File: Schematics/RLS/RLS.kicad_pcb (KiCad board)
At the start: 4 copper layers, 228.6 x 228.6 mm, 121 parts, among them J1 Velleman_Probe1, J2 Velleman_Probe2, J3 Velleman_FuncGen, J4 Logic_Analyzer1, J5 Logic_Analyzer2, J6 ADS1115, J7 DC_Fan, Q1 BS170, U1 ARDUINO_MEGA_SHIELD, U10 LT1963, U11 LT1963, U12 ULN2803A, U13 RA30421051, U14 RA30421051, U15 RB496EATR, U16 RB496EATR, U17 NE5532, U18 NE5532, U19 RB496EATR, U2 LM317T, U20 RB496EATR, U21 NE5532, U3 LM337T, U4 AD5293, U5 AD5293, U6 LT3015, U7 LT3015, U8 AD5293, U9 AD5293

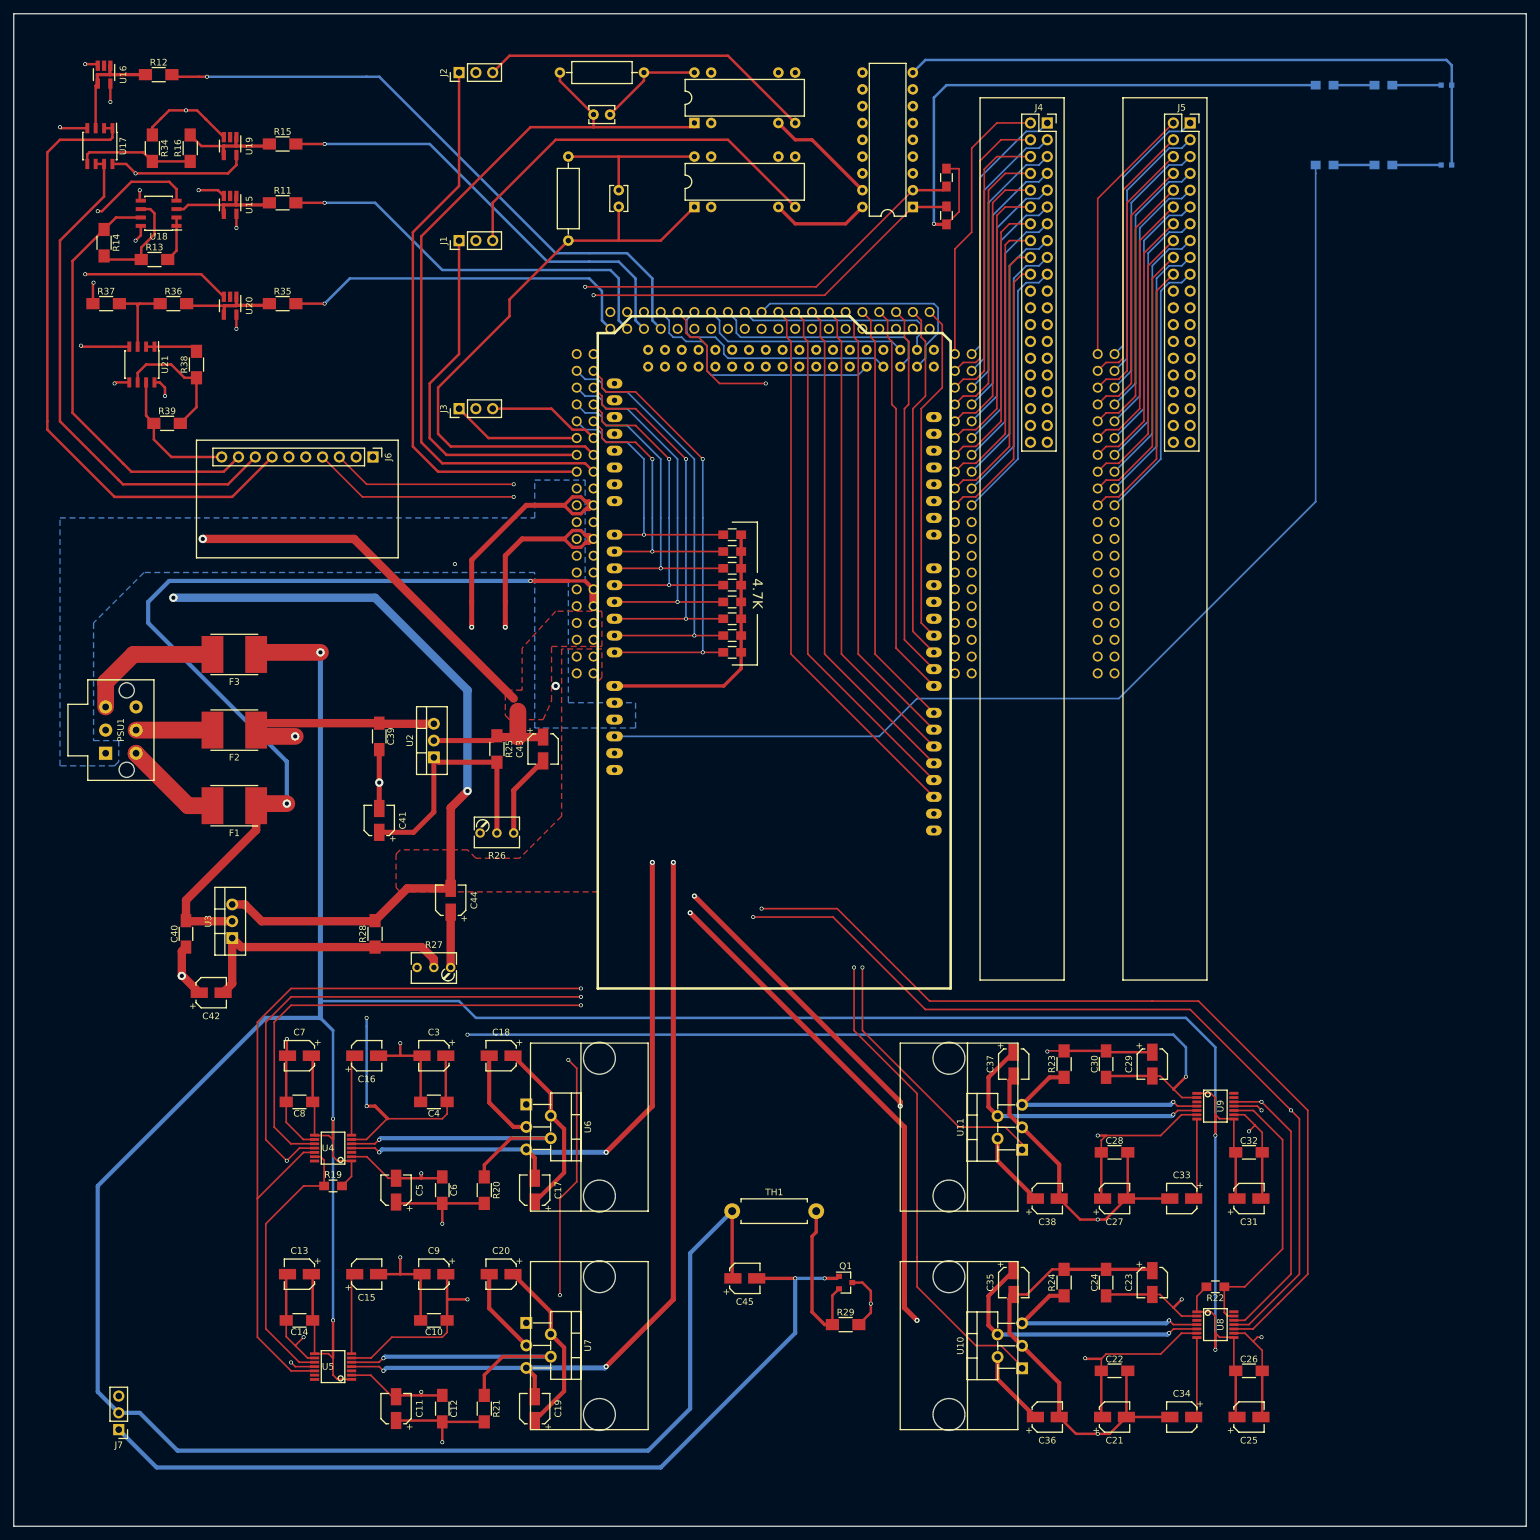
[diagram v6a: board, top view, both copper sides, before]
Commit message: Added Things and Fixed Schematic
Added pots to schematic and pcb for adc balancing.
Fixed the component annotation and netlist in the pcb.
Shrunk the pcb down a bit.
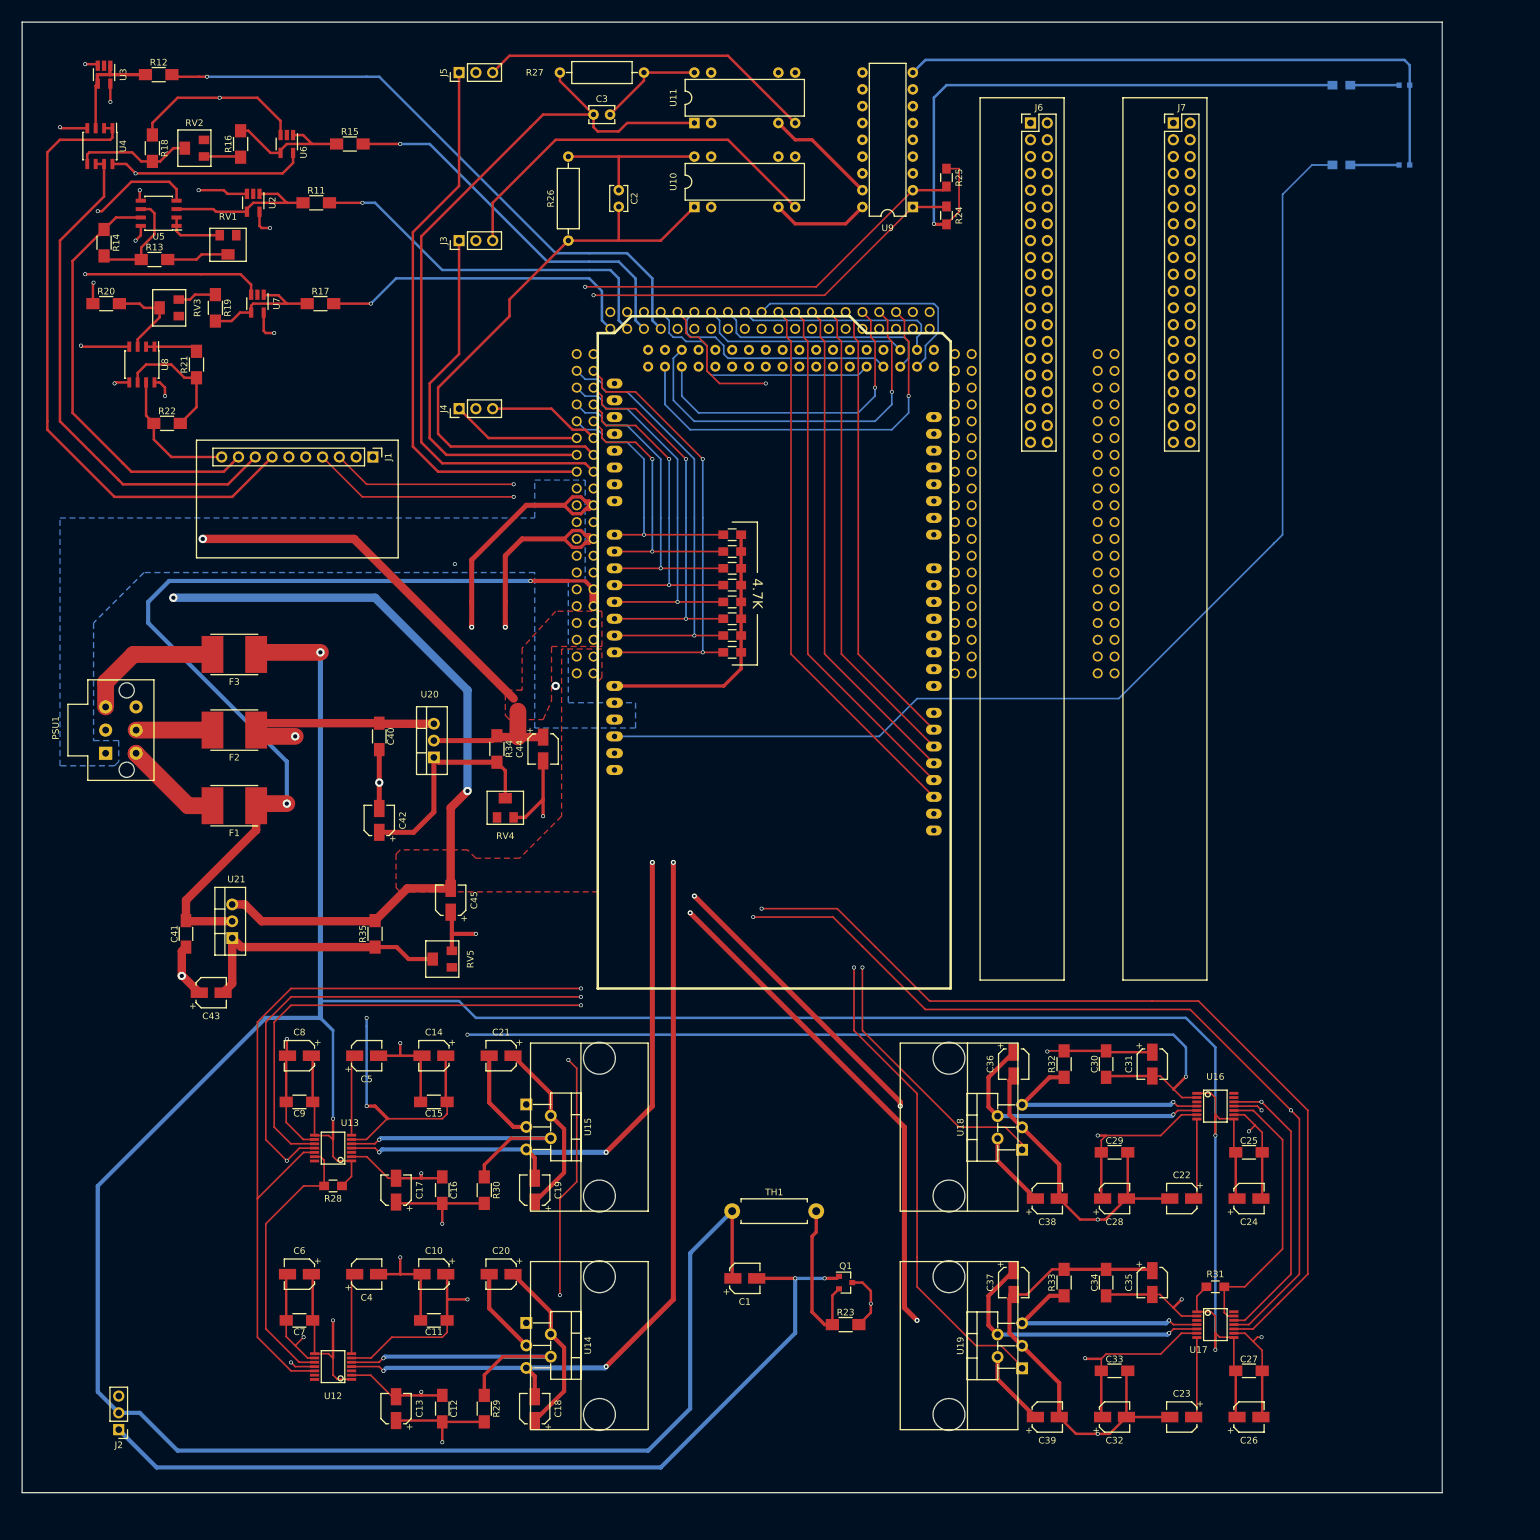
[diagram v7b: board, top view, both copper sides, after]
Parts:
- removed the J1 at (97.8, 54.6)
- removed the J2 at (97.8, 29.2)
- removed the R32 at (228.6, 43.2)
- removed the R33 at (228.6, 31.1)
- added J6: Logic_Analyzer1, Pin_Headers:Pin_Header_Straight_2x20_Pitch2.54mm, F.Cu at (184.2, 36.8)
- added J7: Logic_Analyzer2, Pin_Headers:Pin_Header_Straight_2x20_Pitch2.54mm, F.Cu at (205.7, 36.8)
- added RV1: 500, RLS_CustomFootprints:Potentiometer_Trimmer_Bourns_PVG5A, F.Cu at (62.9, 55.2)
- added RV2: 500, RLS_CustomFootprints:Potentiometer_Trimmer_Bourns_PVG5A, F.Cu at (57.8, 40.6)
- added RV3: 500, RLS_CustomFootprints:Potentiometer_Trimmer_Bourns_PVG5A, F.Cu at (54.0, 64.8)
- J3: value Velleman_FuncGen -> Velleman_Probe1
- J4: value Logic_Analyzer1 -> Velleman_FuncGen; footprint Pin_Headers:Pin_Header_Straight_2x20_Pitch2.54mm -> Pin_Headers:Pin_Header_Straight_1x03_Pitch2.54mm
- J5: value Logic_Analyzer2 -> Velleman_Probe2; footprint Pin_Headers:Pin_Header_Straight_2x20_Pitch2.54mm -> Pin_Headers:Pin_Header_Straight_1x03_Pitch2.54mm
- R13: value 1K -> 768
- R16: value 10K -> 9.76K
- R19: renamed from R36; value 10K -> 9.76K
- RV4: renamed from R26; value 1K_POT -> 1K; footprint Potentiometers:Potentiometer_Trimmer_Bourns_3266Y -> RLS_CustomFootprints:Potentiometer_Trimmer_Bourns_PVG5A
- RV5: renamed from R27; value 1K_POT -> 1K; footprint Potentiometers:Potentiometer_Trimmer_Bourns_3266Y -> RLS_CustomFootprints:Potentiometer_Trimmer_Bourns_PVG5A
- moved J5 105.7 mm to (97.8, 29.2), turned to 90 degrees
- moved J4 96.6 mm to (97.8, 80.0), turned to 90 degrees
- moved J3 25.4 mm to (97.8, 54.6)
- moved R15 10.2 mm to (81.3, 40.0)
- moved U6 8.58 mm to (71.8, 40.0)
- moved R16 7.65 mm to (64.8, 40.0)
- moved R19 6.38 mm to (61.0, 64.8), turned to 270 degrees
- moved R1 6.35 mm to (231.1, 43.2)
- moved R2 6.35 mm to (231.1, 31.1)
- moved D1 6.35 mm to (240.7, 43.2)
- moved D2 6.35 mm to (240.7, 31.1)
- moved R17 5.71 mm to (76.8, 64.1)
- moved RV4 5.39 mm to (104.8, 140.3), turned to 0 degrees
- moved R11 5.08 mm to (76.2, 48.9)
- moved U7 4.14 mm to (67.3, 64.1)
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- renumbered C45 to C1, C9 to C10, C10 to C11, C11 to C13, C3 to C14, C4 to C15, C6 to C16, C5 to C17, C19 to C18, C17 to C19, C1 to C2, C18 to C21, C33 to C22, C34 to C23, C31 to C24, C32 to C25, C25 to C26, C26 to C27, C27 to C28, C28 to C29, C2 to C3, C29 to C31, C21 to C32, C22 to C33, C24 to C34, C23 to C35, C37 to C36, C35 to C37, C36 to C39, C15 to C4, C39 to C40, C40 to C41, C41 to C42, C42 to C43, C43 to C44, C44 to C45, C16 to C5, C13 to C6, C14 to C7, C7 to C8, C8 to C9, J6 to J1, J7 to J2, R30 to R1, R35 to R17, R34 to R18, R31 to R2, R37 to R20, R38 to R21, R39 to R22, R29 to R23, R1 to R24, R2 to R25, R17 to R26, R18 to R27, R19 to R28, R21 to R29, R20 to R30, R22 to R31, R23 to R32, R24 to R33, R25 to R34, R28 to R35, U13 to U10, U14 to U11, U5 to U12, U4 to U13, U7 to U14, U6 to U15, U9 to U16, U8 to U17, U11 to U18, U10 to U19, U15 to U2, U2 to U20, U3 to U21, U16 to U3, U17 to U4, U18 to U5, U19 to U6, U20 to U7, U21 to U8, U12 to U9
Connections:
- DB1 pad 42: AD4 -> SCL
- DB1 pad 44: AD5 -> SDA
- DB1 pad 46: AD6 -> SCLK
- DB1 pad 48: AD7 -> MOSI
- DB1 pad 50: AD8 -> MISO
- J3 pad 1: NEG_GEN -> NEG_SCP1
- J3 pad 3: POS_GEN -> /Scope_Probe_Gain/+SCP1
- J4 pad 1: L1D0 -> NEG_GEN
- J4 pad 2: L1D1 -> Net-(J4-Pad2)
- J4 pad 3: L1D2 -> POS_GEN
- J5 pad 1: L2D0 -> NEG_SCP2
- J5 pad 2: L2D1 -> Net-(J5-Pad2)
- J5 pad 3: L2D2 -> /Scope_Probe_Gain/+SCP2
- R1 pad 1: /ARD_R -> AD_LED
- R13 pad 2: /ADC_Divder_&_DC_Fan/-5_BUFF -> /ADC_Divder_&_DC_Fan/-5_ADJ
- R16 pad 1: /ADC_Divder_&_DC_Fan/+15_DIV -> /ADC_Divder_&_DC_Fan/+15_ADJ
- R19 pad 1: /ADC_Divder_&_DC_Fan/-15_DIV -> /ADC_Divder_&_DC_Fan/-15_ADJ
- R2 pad 1: /PSU_R -> +5V
- RV5 pad 1: AGND -> Net-(RV5-Pad1)
- RV5 pad 3: Net-(R27-Pad3) -> AGND
- U1 pad 4: AD4 -> Net-(U1-Pad4)
- U1 pad 48: Net-(U1-Pad48) -> P_POT_CE
- U1 pad 5: AD5 -> Net-(U1-Pad5)
- U1 pad 50: P_POT_CE -> MISO
- U1 pad 6: AD6 -> Net-(U1-Pad6)
- U1 pad 7: AD7 -> Net-(U1-Pad7)
- U1 pad 8: AD8 -> Net-(U1-Pad8)
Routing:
- net L1GND: track 248.7 -> 0.00 mm
- net L2GND: track 243.5 -> 0.00 mm
- net AD8: track 65.1 -> 0.00 mm
- net SCLK: track 376.8 -> 438.0 mm, vias 6 -> 7
- net AD7: track 59.9 -> 0.00 mm
- net MOSI: track 332.5 -> 390.8 mm, vias 2 -> 3
- net AD6: track 56.9 -> 0.00 mm
- net AD5: track 54.3 -> 0.00 mm
- net AD4: track 51.8 -> 0.00 mm
- net MISO: track 0.00 -> 49.2 mm, vias 0 -> 1
- net L1D17: track 44.1 -> 0.00 mm
- net L1D5: track 43.8 -> 0.00 mm
- net L1D19: track 43.8 -> 0.00 mm
- net L1D3: track 43.4 -> 0.00 mm
- net L1D21: track 43.4 -> 0.00 mm
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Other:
- board size 228.6 x 228.6 mm -> 214.6 x 222.2 mm

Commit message: MAJOR CHANGE! READ BELOW
Due to layout issues, I changed the pins used for the variable regulator shutdown lines. +V1_SHDN is now AA9, +V2_SHDN is now AA8, -V1_SHDN is now AA11, and -V2_SHDN is now AA10. MAKE SURE TO CHANGE THE RESPECTIVE CODE (Paolo).

Included in this upload is the pre-design review finish PCB and Schematic, with pdf files of each for printing and easy reference.
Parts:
- added REF**: MountingHole_3.5mm, Mounting_Holes:MountingHole_3.5mm, F.Cu at (167.6, 52.7)
- added REF**: MountingHole_3.5mm, Mounting_Holes:MountingHole_3.5mm, F.Cu at (55.2, 52.7)
- added REF**: MountingHole_3.5mm, Mounting_Holes:MountingHole_3.5mm, F.Cu at (167.6, 145.4)
- added REF**: MountingHole_3.5mm, Mounting_Holes:MountingHole_3.5mm, F.Cu at (55.2, 145.4)
- added REF**: MountingHole_3.5mm, Mounting_Holes:MountingHole_3.5mm, F.Cu at (115.6, 182.2)
- U12, U13, U16, U17: footprint SMD_Packages:SSOP-14 -> Housings_SSOP:TSSOP-14_4.4x5mm_Pitch0.65mm
- moved J2 38.9 mm to (24.8, 201.9)
- moved D1 38.1 mm to (203.2, 36.2)
- moved D2 38.1 mm to (203.2, 24.1)
- moved R1 38.1 mm to (193.7, 36.2)
- moved R2 38.1 mm to (193.7, 24.1)
- moved C34 27.0 mm to (169.5, 205.1)
- moved C37 27.0 mm to (155.6, 205.1)
- moved C30 27.0 mm to (169.5, 172.1)
- moved C36 27.0 mm to (155.6, 172.1)
- moved C11 27.0 mm to (67.9, 210.8)
- moved C14 27.0 mm to (67.9, 170.8)
- moved J3 27.0 mm to (71.8, 47.6)
- moved J4 27.0 mm to (71.8, 73.0)
- moved R27 27.0 mm to (99.7, 22.2)
- moved RV4 27.0 mm to (78.7, 133.3)
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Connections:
- J1 pad 6: Net-(J1-Pad6) -> (no net)
- J2 pad 3: Net-(J2-Pad3) -> (no net)
- J3 pad 2: Net-(J3-Pad2) -> (no net)
- J4 pad 2: Net-(J4-Pad2) -> (no net)
- J5 pad 2: Net-(J5-Pad2) -> (no net)
- RV1 pad 1: Net-(RV1-Pad1) -> (no net)
- RV2 pad 3: Net-(RV2-Pad3) -> (no net)
- RV3 pad 1: Net-(RV3-Pad1) -> (no net)
- RV4 pad 1: Net-(RV4-Pad1) -> (no net)
- RV5 pad 1: Net-(RV5-Pad1) -> (no net)
- U1 pad 0: Net-(U1-Pad0) -> (no net)
- U1 pad 1: Net-(U1-Pad1) -> (no net)
- U1 pad 14: Net-(U1-Pad14) -> (no net)
- U1 pad 15: Net-(U1-Pad15) -> (no net)
- U1 pad 16: Net-(U1-Pad16) -> (no net)
- U1 pad 17: Net-(U1-Pad17) -> (no net)
- U1 pad 18: Net-(U1-Pad18) -> (no net)
- U1 pad 19: Net-(U1-Pad19) -> (no net)
- U1 pad 2: Net-(U1-Pad2) -> (no net)
- U1 pad 3: Net-(U1-Pad3) -> (no net)
- U1 pad 3V3: Net-(U1-Pad3V3) -> (no net)
- U1 pad 4: Net-(U1-Pad4) -> (no net)
- U1 pad 49: Net-(U1-Pad49) -> (no net)
- U1 pad 5: Net-(U1-Pad5) -> (no net)
- U1 pad 5V_4: Net-(U1-Pad5V_4) -> (no net)
- U1 pad 5V_5: Net-(U1-Pad5V_5) -> (no net)
- U1 pad 6: Net-(U1-Pad6) -> (no net)
- U1 pad 7: Net-(U1-Pad7) -> (no net)
- U1 pad 8: Net-(U1-Pad8) -> (no net)
- U1 pad AD10: -V1_SHDN -> -V2_SHDN
- U1 pad AD11: -V2_SHDN -> -V1_SHDN
- U1 pad AD8: +V1_SHDN -> +V2_SHDN
- U1 pad AD9: +V2_SHDN -> +V1_SHDN
- U1 pad AREF: Net-(U1-PadAREF) -> (no net)
- U1 pad GND2: Net-(U1-PadGND2) -> (no net)
- U1 pad GND3: Net-(U1-PadGND3) -> (no net)
- U1 pad GND4: Net-(U1-PadGND4) -> (no net)
- U1 pad GND5: Net-(U1-PadGND5) -> (no net)
- U1 pad RST: Net-(U1-PadRST) -> (no net)
- U10 pad 5: Net-(U10-Pad5) -> (no net)
- U10 pad 6: Net-(U10-Pad6) -> (no net)
- U10 pad 7: Net-(U10-Pad7) -> (no net)
- U11 pad 5: Net-(U11-Pad5) -> (no net)
- U11 pad 6: Net-(U11-Pad6) -> (no net)
- U11 pad 7: Net-(U11-Pad7) -> (no net)
- U12 pad 13: Net-(U12-Pad13) -> (no net)
- U12 pad 14: Net-(U12-Pad14) -> (no net)
- U12 pad 3: Net-(U12-Pad3) -> (no net)
- U13 pad 14: Net-(U13-Pad14) -> (no net)
- U13 pad 3: Net-(U13-Pad3) -> (no net)
- U16 pad 13: Net-(U16-Pad13) -> (no net)
- U16 pad 14: Net-(U16-Pad14) -> (no net)
- U16 pad 3: Net-(U16-Pad3) -> (no net)
- U17 pad 14: Net-(U17-Pad14) -> (no net)
- U17 pad 3: Net-(U17-Pad3) -> (no net)
- U2 pad 2: Net-(U2-Pad2) -> (no net)
- U3 pad 2: Net-(U3-Pad2) -> (no net)
- U6 pad 2: Net-(U6-Pad2) -> (no net)
- U7 pad 2: Net-(U7-Pad2) -> (no net)
- U9 pad 11: Net-(U9-Pad11) -> (no net)
- U9 pad 12: Net-(U9-Pad12) -> (no net)
- U9 pad 13: Net-(U9-Pad13) -> (no net)
- U9 pad 14: Net-(U9-Pad14) -> (no net)
- U9 pad 15: Net-(U9-Pad15) -> (no net)
- U9 pad 16: Net-(U9-Pad16) -> (no net)
- U9 pad 3: Net-(U9-Pad3) -> (no net)
- U9 pad 4: Net-(U9-Pad4) -> (no net)
- U9 pad 5: Net-(U9-Pad5) -> (no net)
- U9 pad 6: Net-(U9-Pad6) -> (no net)
- U9 pad 7: Net-(U9-Pad7) -> (no net)
- U9 pad 8: Net-(U9-Pad8) -> (no net)
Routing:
- net L2GND: track 0.00 -> 250.7 mm
- net L1GND: track 0.00 -> 250.7 mm
- net +5V: track 796.9 -> 728.4 mm
- net -5V_R: track 190.2 -> 245.5 mm
- net L2CLK2: track 0.00 -> 47.3 mm
- net L1CLK2: track 0.00 -> 47.3 mm
- net L2D25: track 0.00 -> 44.4 mm
- net L2D19: track 0.00 -> 44.4 mm
- net L2D11: track 0.00 -> 44.4 mm
- net L2D9: track 0.00 -> 44.4 mm
- net L2D7: track 0.00 -> 44.4 mm
- net L2D29: track 0.00 -> 44.4 mm
- net L2D23: track 0.00 -> 44.4 mm
- net L2D15: track 0.00 -> 44.4 mm
- net L1D15: track 0.00 -> 44.4 mm
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- removed copper zone on Upper, net +15V
- removed copper zone on F.Cu, net +5V_R
- removed copper zone on F.Cu, net -5V_R
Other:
- board size 214.6 x 222.2 mm -> 200.7 x 215.9 mm
- board text removed: "O"
